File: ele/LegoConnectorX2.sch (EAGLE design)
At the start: 6 parts, among them X1 NXT-SOCKET, X2 NXT-SOCKET

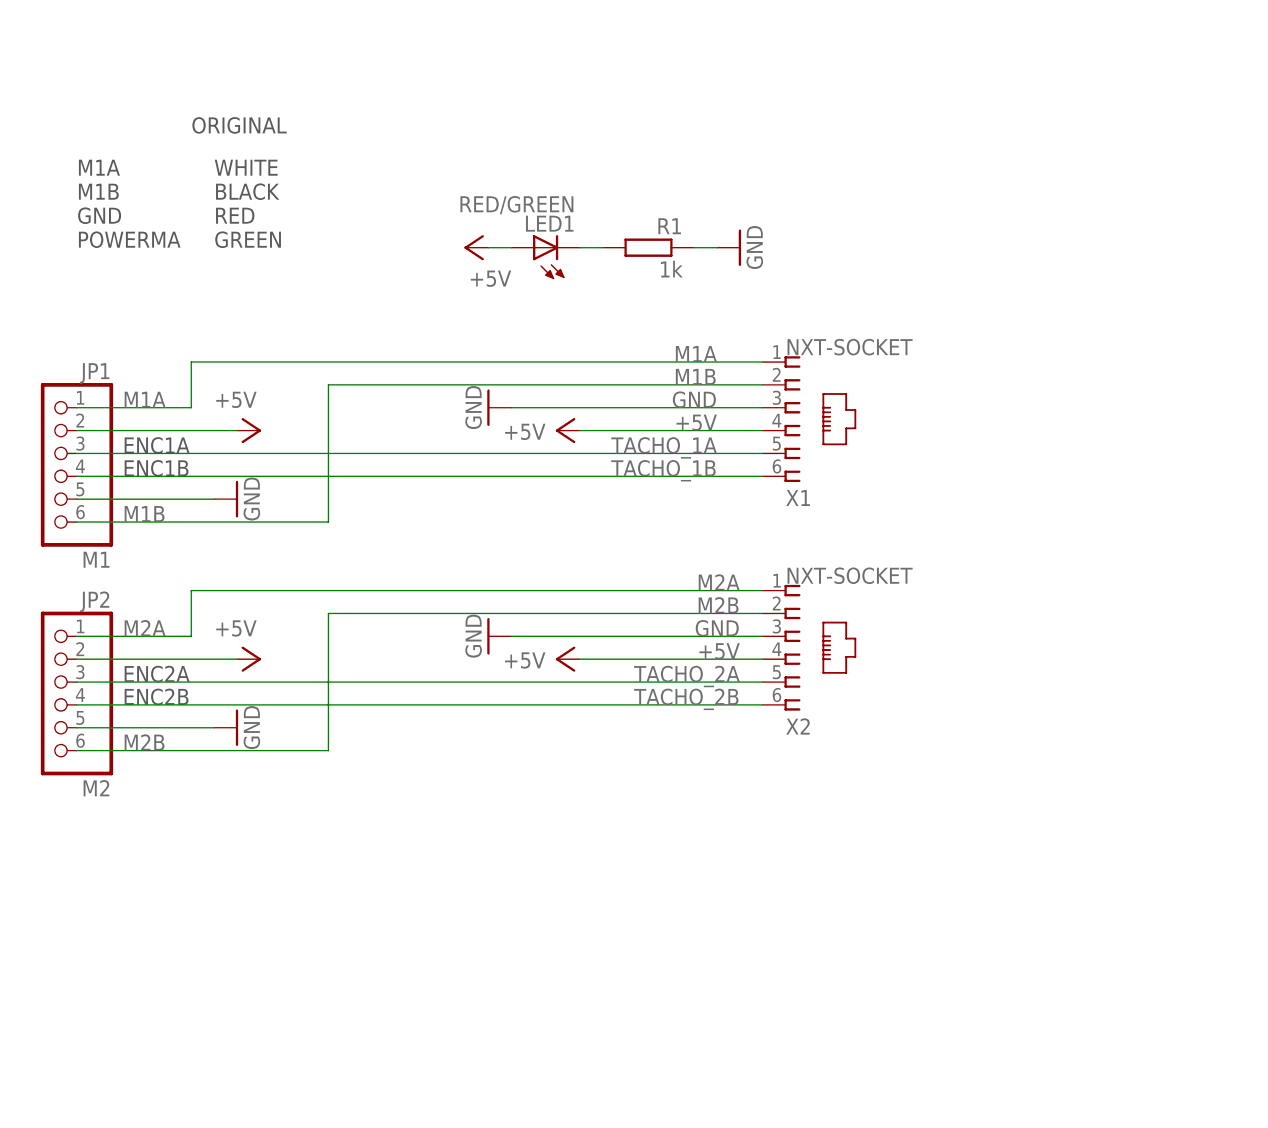
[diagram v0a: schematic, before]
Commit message: Add licenses to Eagle files
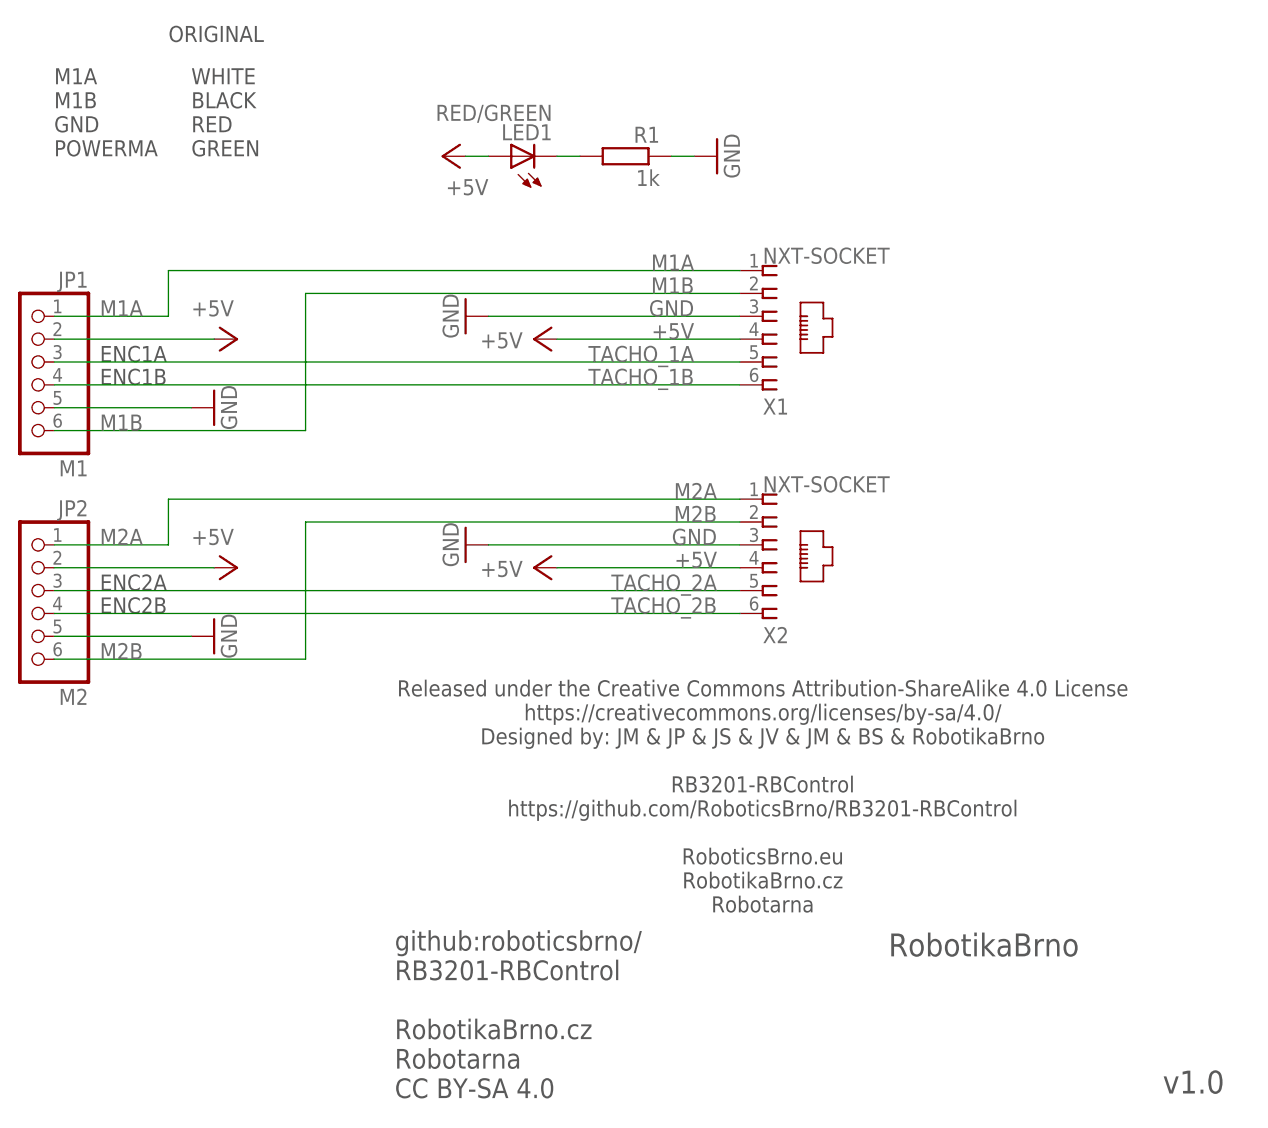
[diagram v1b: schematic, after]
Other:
- note added: "Released under the Creative Commons Attribution-ShareAlike 4.0 License https://creativecommons.org/licenses/by-sa/4.0/ Designed by: JM & JP & JS & JV & JM & BS & RobotikaBrno RB3201-RBControl https://github.com/RoboticsBrno/RB3201-RBControl RoboticsBrno.eu RobotikaBrno.cz Robotarna"
- note added: "RobotikaBrno"
- note added: "github:roboticsbrno/ RB3201-RBControl RobotikaBrno.cz Robotarna CC BY-SA 4.0"
- note added: "v1.0"
- moved on the sheet: JP1, JP2, LED1, R1, X1, X2
